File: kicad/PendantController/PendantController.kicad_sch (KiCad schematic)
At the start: 1 part, among them U1 Arduino_Micro

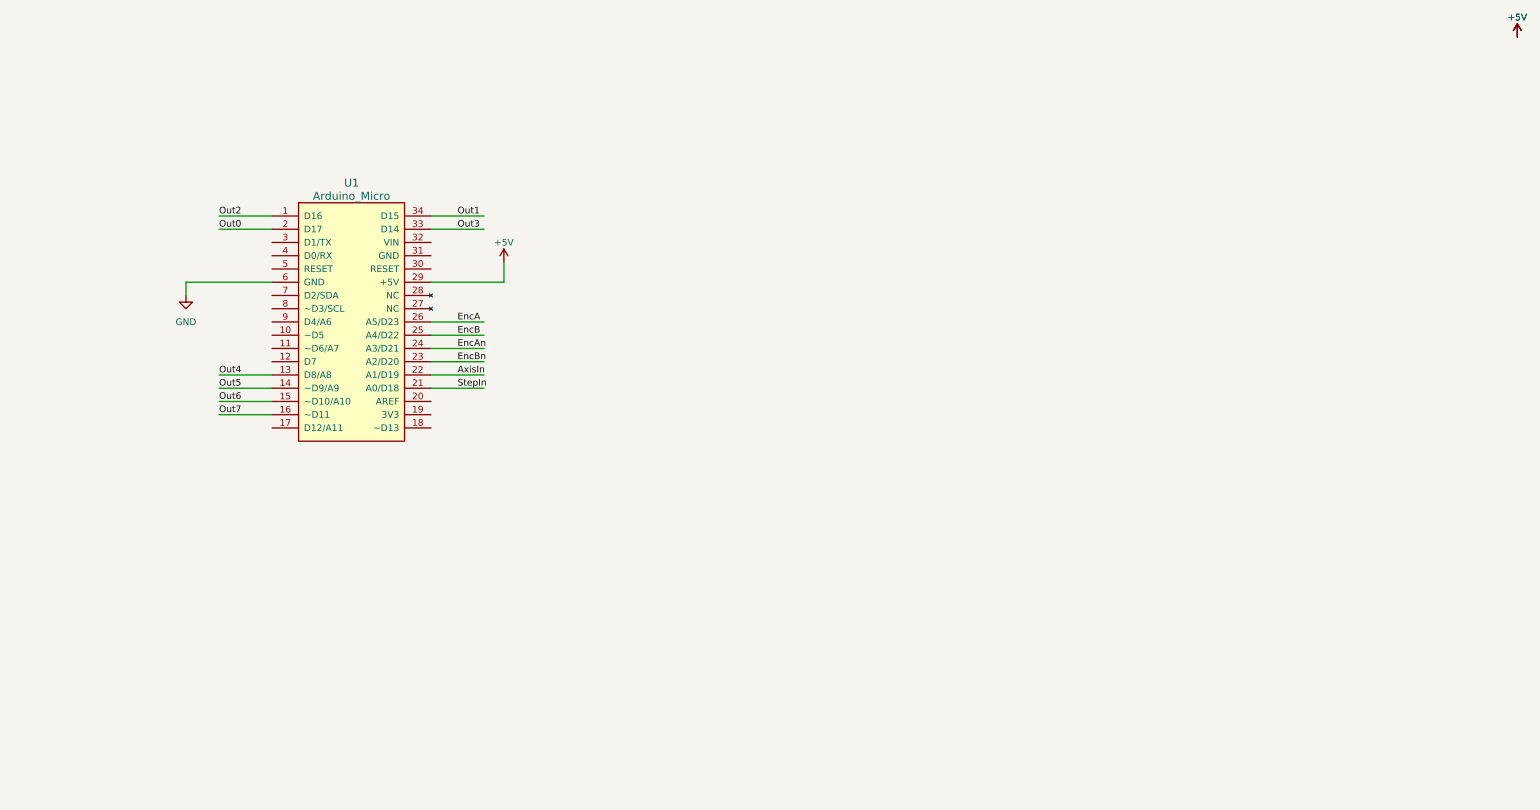
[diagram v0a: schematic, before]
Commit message: Added IO breakout board PCB and case bottom cover
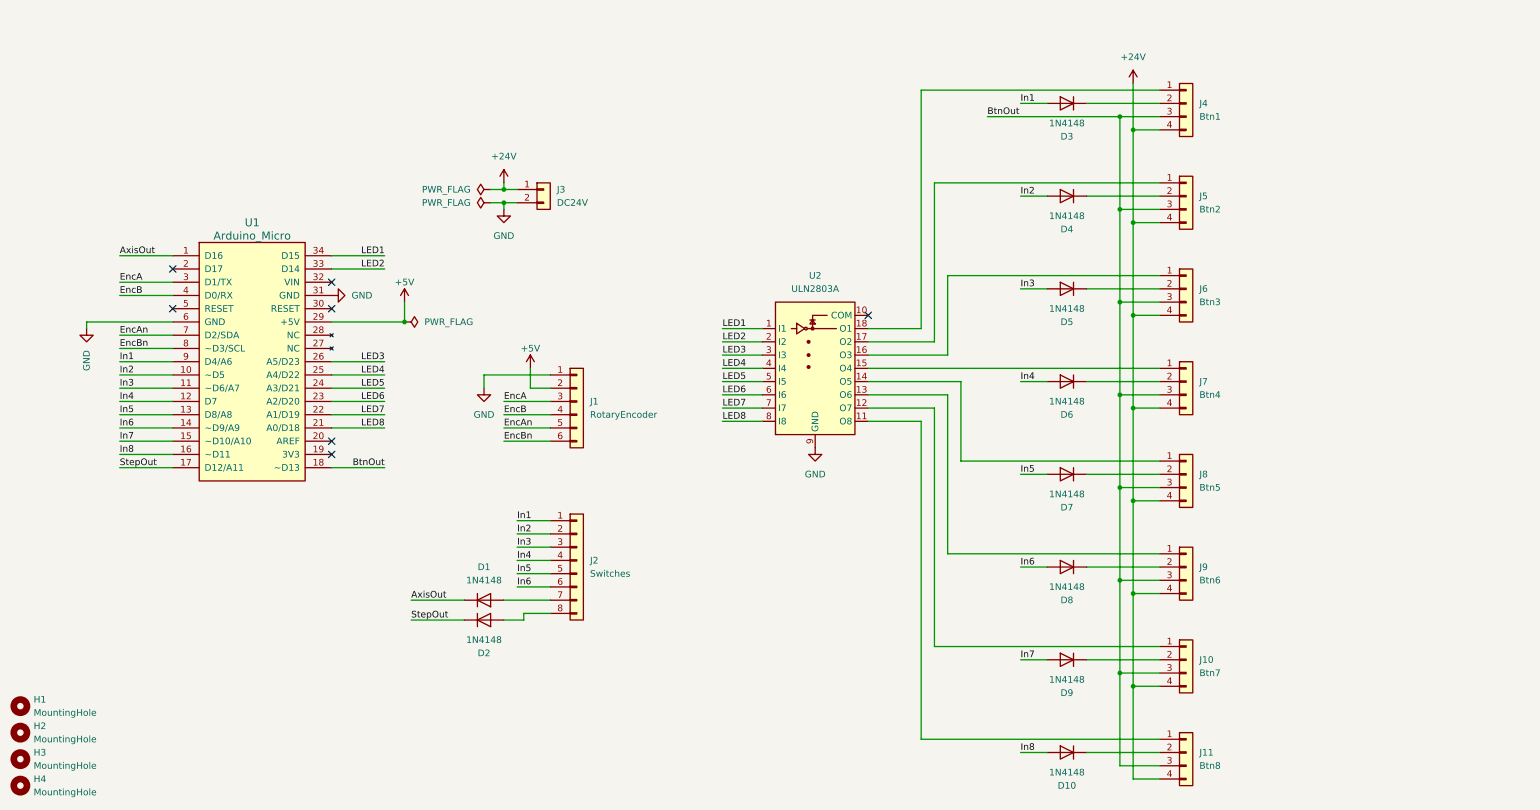
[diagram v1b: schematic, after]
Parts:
- added D1, D10, D2, D3, D4, D5, D6, D7, D8, D9: 1N4148, Diode_THT:D_DO-35_SOD27_P7.62mm_Horizontal, symbol Diode:1N4148
- added H1, H2, H3, H4: MountingHole, MountingHole:MountingHole_3.2mm_M3, symbol Mechanical:MountingHole
- added J1: RotaryEncoder, Connector_PinHeader_2.54mm:PinHeader_1x06_P2.54mm_Vertical, symbol Connector_Generic:Conn_01x06
- added J10: Btn7, Connector_JST:JST_XH_B4B-XH-A_1x04_P2.50mm_Vertical, symbol Connector_Generic:Conn_01x04
- added J11: Btn8, Connector_JST:JST_XH_B4B-XH-A_1x04_P2.50mm_Vertical, symbol Connector_Generic:Conn_01x04
- added J2: Switches, Connector_PinHeader_2.54mm:PinHeader_1x08_P2.54mm_Vertical, symbol Connector_Generic:Conn_01x08
- added J3: DC24V, Connector_PinHeader_2.54mm:PinHeader_1x02_P2.54mm_Vertical, symbol Connector_Generic:Conn_01x02
- added J4: Btn1, Connector_JST:JST_XH_B4B-XH-A_1x04_P2.50mm_Vertical, symbol Connector_Generic:Conn_01x04
- added J5: Btn2, Connector_JST:JST_XH_B4B-XH-A_1x04_P2.50mm_Vertical, symbol Connector_Generic:Conn_01x04
- added J6: Btn3, Connector_JST:JST_XH_B4B-XH-A_1x04_P2.50mm_Vertical, symbol Connector_Generic:Conn_01x04
- added J7: Btn4, Connector_JST:JST_XH_B4B-XH-A_1x04_P2.50mm_Vertical, symbol Connector_Generic:Conn_01x04
- added J8: Btn5, Connector_JST:JST_XH_B4B-XH-A_1x04_P2.50mm_Vertical, symbol Connector_Generic:Conn_01x04
- added J9: Btn6, Connector_JST:JST_XH_B4B-XH-A_1x04_P2.50mm_Vertical, symbol Connector_Generic:Conn_01x04
- added U2: ULN2803A, Package_DIP:DIP-18_W7.62mm, symbol Transistor_Array:ULN2803A
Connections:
- net +5V: now also J1.2 (Pin_2)
- net EncA: now also U1.3 (D1/TX), J1.3 (Pin_3); no longer U1.26 (A5/D23)
- net EncAn: now also U1.7 (D2/SDA), J1.5 (Pin_5); no longer U1.24 (A3/D21)
- net EncB: now also U1.4 (D0/RX), J1.4 (Pin_4); no longer U1.25 (A4/D22)
- net EncBn: now also U1.8 (~D3/SCL), J1.6 (Pin_6); no longer U1.23 (A2/D20)
- net GND: now also U1.31 (GND), J1.1 (Pin_1), J3.2 (Pin_2), U2.9 (GND)
- net In2: now reaches U1.10 (~D5)
- net In2: now also D4.2 (A), J2.2 (Pin_2)
- net In3: now reaches U1.11 (~D6/A7)
- net In3: now also D5.2 (A), J2.3 (Pin_3)
- net In4: now reaches U1.12 (D7)
- net In4: now also D6.2 (A), J2.4 (Pin_4)
- net StepOut: now reaches U1.17 (D12/A11)
- net StepOut: now also D2.1 (K)
- net BtnOut: now reaches U1.18 (~D13)
- net BtnOut: now also J10.3 (Pin_3), J11.3 (Pin_3), J4.3 (Pin_3), J5.3 (Pin_3), J6.3 (Pin_3), J7.3 (Pin_3), J8.3 (Pin_3), J9.3 (Pin_3)
- net In1: now reaches U1.9 (D4/A6)
- net In1: now also D3.2 (A), J2.1 (Pin_1)
- net AxisIn renamed LED7
- net LED7: now also U2.7 (I7)
- net Out0: no longer names the net of U1.2 (D17)
- net Out1 renamed LED1
- net LED1: now also U2.1 (I1)
- net Out2 renamed AxisOut
- net AxisOut: now also D1.1 (K)
- net Out3 renamed LED2
- net LED2: now also U2.2 (I2)
- net Out4 renamed In5
- net In5: now also D7.2 (A), J2.5 (Pin_5)
- net Out5 renamed In6
- net In6: now also D8.2 (A), J2.6 (Pin_6)
- net Out6 renamed In7
- net In7: now also D9.2 (A)
- net Out7 renamed In8
- net In8: now also D10.2 (A)
- net StepIn renamed LED8
- net LED8: now also U2.8 (I8)
- new net: J10.1 (Pin_1), U2.12 (O7)
- new net: D9.1 (K), J10.2 (Pin_2)
- new net: D5.1 (K), J6.2 (Pin_2)
- new net: D8.1 (K), J9.2 (Pin_2)
- new net: J7.1 (Pin_1), U2.15 (O4)
- new net: D6.1 (K), J7.2 (Pin_2)
- new net: D10.1 (K), J11.2 (Pin_2)
- new net: D4.1 (K), J5.2 (Pin_2)
- new net: D2.2 (A), J2.8 (Pin_8)
- new net: D1.2 (A), J2.7 (Pin_7)
- new net: D7.1 (K), J8.2 (Pin_2)
- new net: D3.1 (K), J4.2 (Pin_2)
- new net: J5.1 (Pin_1), U2.17 (O2)
- new net: J6.1 (Pin_1), U2.16 (O3)
- new net: J9.1 (Pin_1), U2.13 (O6)
- new net: J8.1 (Pin_1), U2.14 (O5)
- new net: J4.1 (Pin_1), U2.18 (O1)
- new net: J11.1 (Pin_1), U2.11 (O8)
- new net +24V: J10.4 (Pin_4), J11.4 (Pin_4), J3.1 (Pin_1), J4.4 (Pin_4), J5.4 (Pin_4), J6.4 (Pin_4), J7.4 (Pin_4), J8.4 (Pin_4), J9.4 (Pin_4)
- new net LED3: U1.26 (A5/D23), U2.3 (I3)
- new net LED4: U1.25 (A4/D22), U2.4 (I4)
- new net LED5: U1.24 (A3/D21), U2.5 (I5)
- new net LED6: U1.23 (A2/D20), U2.6 (I6)
- no-connect marks 0 -> 7
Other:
- moved on the sheet: U1

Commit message: Updated PCB layout
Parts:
- added R1: 10, Resistor_THT:R_Axial_DIN0309_L9.0mm_D3.2mm_P12.70mm_Horizontal, symbol Device:R
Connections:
- net GND: now also R1.2; no longer J3.2 (Pin_2)
- new net: J3.2 (Pin_2), R1.1
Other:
- moved on the sheet: J3
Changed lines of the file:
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@@
 	(wire
 		(pts
-			(xy 128.27 45.72) (xy 130.81 45.72)
+			(xy 128.27 45.72) (xy 138.43 45.72)
 		)
 		(stroke
@@
 	(symbol
 		(lib_id "Connector_Generic:Conn_01x02")
-		(at 135.89 45.72 0)
+		(at 143.51 45.72 0)
 		(unit 1)
 		(exclude_from_sim no)
@@
 		(fields_autoplaced yes)
 		(property "Reference" "J3"
-			(at 138.43 45.7199 0)
+			(at 146.05 45.7199 0)
 			(effects
 				(font
@@
 		)
 		(property "Value" "DC24V"
-			(at 138.43 48.2599 0)
+			(at 146.05 48.2599 0)
 			(effects
 				(font
@@
 		)
 		(property "Footprint" "Connector_PinHeader_2.54mm:PinHeader_1x02_P2.54mm_Vertical"
-			(at 135.89 45.72 0)
+			(at 143.51 45.72 0)
 			(effects
 				(font
@@
 		)
 		(property "Datasheet" "~"
-			(at 135.89 45.72 0)
+			(at 143.51 45.72 0)
 			(effects
 				(font
@@
 		)
 		(property "Description" "Generic connector, single row, 01x02, script generated (kicad-library-utils/schlib/autogen/connector/)"
-			(at 135.89 45.72 0)
+			(at 143.51 45.72 0)
 			(effects
 				(font
@@
 					(unit 1)
 				)
+			)
+		)
+	)
+	(symbol
+		(lib_id "Device:R")
+		(at 134.62 48.26 270)
+		(unit 1)
+		(exclude_from_sim no)
+		(in_bom yes)
+		(on_board yes)
+		(dnp no)
+		(property "Reference" "R1"
+			(at 134.62 54.61 90)
+			(effects
+				(font
+					(size 1.27 1.27)
+				)
+			)
+		)
+		(property "Value" "10"
+			(at 134.62 52.07 90)
+			(effects
+				(font
+					(size 1.27 1.27)
+				)
+			)
+		)
+		(property "Footprint" "Resistor_THT:R_Axial_DIN0309_L9.0mm_D3.2mm_P12.70mm_Horizontal"
+			(at 134.62 46.482 90)
+			(effects
+				(font
+					(size 1.27 1.27)
+				)
+				(hide yes)
+			)
+		)
+		(property "Datasheet" "~"
+			(at 134.62 48.26 0)
+			(effects
+				(font
+					(size 1.27 1.27)
+				)
+				(hide yes)
+			)
+		)
+		(property "Description" "Resistor"
+			(at 134.62 48.26 0)
+			(effects
+				(font
+					(size 1.27 1.27)
+				)
+				(hide yes)
+			)
+		)
+		(pin "1"
+		)
+		(pin "2"
+		)
+		(instances
+			(project "PendantController"
+				(path "/97d16841-8b77-4c29-a79d-2680519e8080"
+					(reference "R1")
+					(unit 1)
+				)
